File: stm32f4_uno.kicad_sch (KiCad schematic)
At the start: 49 parts, among them J101 STM32 GPIO, J102 Digital/PWM, J103 STM32 GPIO, J104 STM32 GPIO, J105 STM32 GPIO, J106 Power, J107 Ethernet, J108 STM32 GPIO, J109 Digital/PWM, J110 Analog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

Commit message: #15 Add all pin sockets
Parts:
- added J111: Conn_01x04, Connector_PinSocket_2.54mm:PinSocket_1x04_P2.54mm_Vertical, symbol Connector_Generic:Conn_01x04
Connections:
- no-connect marks 5 -> 9
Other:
- moved on the sheet: J101, J103, J105, J106, J108, J110

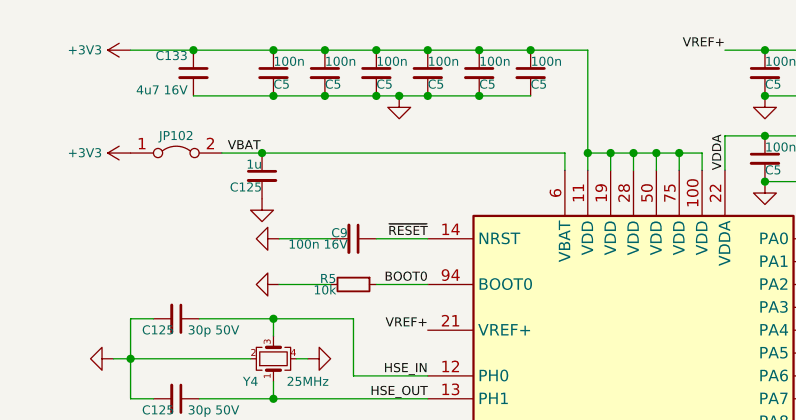
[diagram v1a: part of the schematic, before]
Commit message: #14 Add optional capacitor for RTC operation
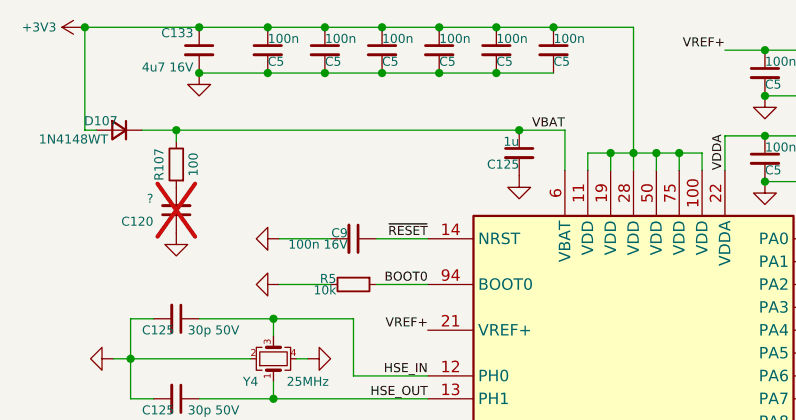
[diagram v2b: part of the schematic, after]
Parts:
- removed JP102: Jumper_2_Bridged, Jumper:SolderJumper-2_P1.3mm_Bridged_RoundedPad1.0x1.5mm, symbol Jumper:Jumper_2_Bridged
- added C120: ?, Capacitor_THT:CP_Radial_D6.3mm_P2.50mm, symbol Device:C_Small
- added D107: 1N4148WT, Diode_SMD:D_SOD-523, symbol Device:D_Small
- added R107: 100, Resistor_SMD:R_0402_1005Metric, symbol Device:R_Small
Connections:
- net +3V3: now also D107.2 (A)
- net GND: now also C120.1
- net VBAT: now also D107.1 (K), R107.2
- new net: C120.2, R107.1
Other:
- moved on the sheet: C125, C133, C5
